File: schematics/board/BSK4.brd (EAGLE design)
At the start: 82 x 100 mm, 32 parts

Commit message: Подписаны разъемы на платах
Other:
- board text added: "to BSK1"
- board text added: "to PAYLOAD"
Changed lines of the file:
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@@
 <text x="54.1" y="4.9" size="1.778" layer="26" rot="MR0">BSK4 "Концерн ИТС"</text>
 <circle x="41" y="50" radius="15.25" width="0.2" layer="20"/>
+<text x="32" y="95" size="1.778" layer="26" rot="MR0">to BSK1</text>
+<text x="45" y="26" size="1.778" layer="26" rot="MR0">to PAYLOAD</text>
 </plain>
 <attributes>

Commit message: Платы подготовлены для Резонита
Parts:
- removed U$10: FS8205A+, CanCubeSat:FS8205A+
- added FS8205A#2: FS8205A+, CanCubeSat:FS8205A+
- moved R5 10.0 mm to (26.0, 21.0)
- moved LED1 9.90 mm to (68.9, 52.5), turned to 90 degrees
- moved R1 9.53 mm to (68.9, 50.6)
- moved LED5 7.32 mm to (26.0, 22.8), turned to 90 degrees
- moved R81 6.75 mm to (68.9, 48.4)
- moved LED4 4.19 mm to (31.3, 75.7)
- moved LED2 3.93 mm to (68.9, 46.5), turned to 270 degrees
- moved R3 2.47 mm to (11.2, 65.6)
- moved LED3 1.17 mm to (12.9, 65.6), turned to 0 degrees
- moved R2 1.00 mm to (25.3, 87.3)
- moved R7 1.00 mm to (25.3, 81.9)
- moved R4 0.51 mm to (33.0, 75.7)
- renumbered U$5 to DS18B20Z, U$8 to L293DD, U$9 to FS8205A#1
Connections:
- removed net HEAT: DS18B20Z.HEAT, FS8205A#1.HEAT, L293DD.HEAT, U$10.HEAT
- net GND: now also DS18B20Z.HEAT, FS8205A#1.HEAT, FS8205A#2.67, FS8205A#2.HEAT, L293DD.HEAT; no longer U$10.67
- net N$4: now also FS8205A#2.4; no longer U$10.4
- net N$6: now also FS8205A#2.5; no longer U$10.5
- net PL-: now also FS8205A#2.23; no longer U$10.23
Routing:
- net GND: track 128.6 -> 75.2 mm, vias 5 -> 2
- net N$27: track 13.8 -> 1.74 mm, vias 2 -> 0
- net 5V: track 165.6 -> 174.7 mm
- net N$3: track 59.1 -> 67.3 mm
- net N$2: track 72.6 -> 76.4 mm
- net PL-: track 76.6 -> 80.3 mm
- net BUS-: track 53.5 -> 50.4 mm
- net N$1: track 66.9 -> 69.2 mm
- net PL_KVCC: track 29.3 -> 30.3 mm
- net N$5: track 1.27 -> 1.94 mm
- net N$28: track 1.30 -> 1.84 mm
- added copper zone on layer 1, net GND
- removed copper zone on layer 1, net HEAT
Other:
- board text added: "BUS"
- board text added: "EM+"
- board text added: "EM-"
- board text added: "HEATER"
- board text added: "PL"

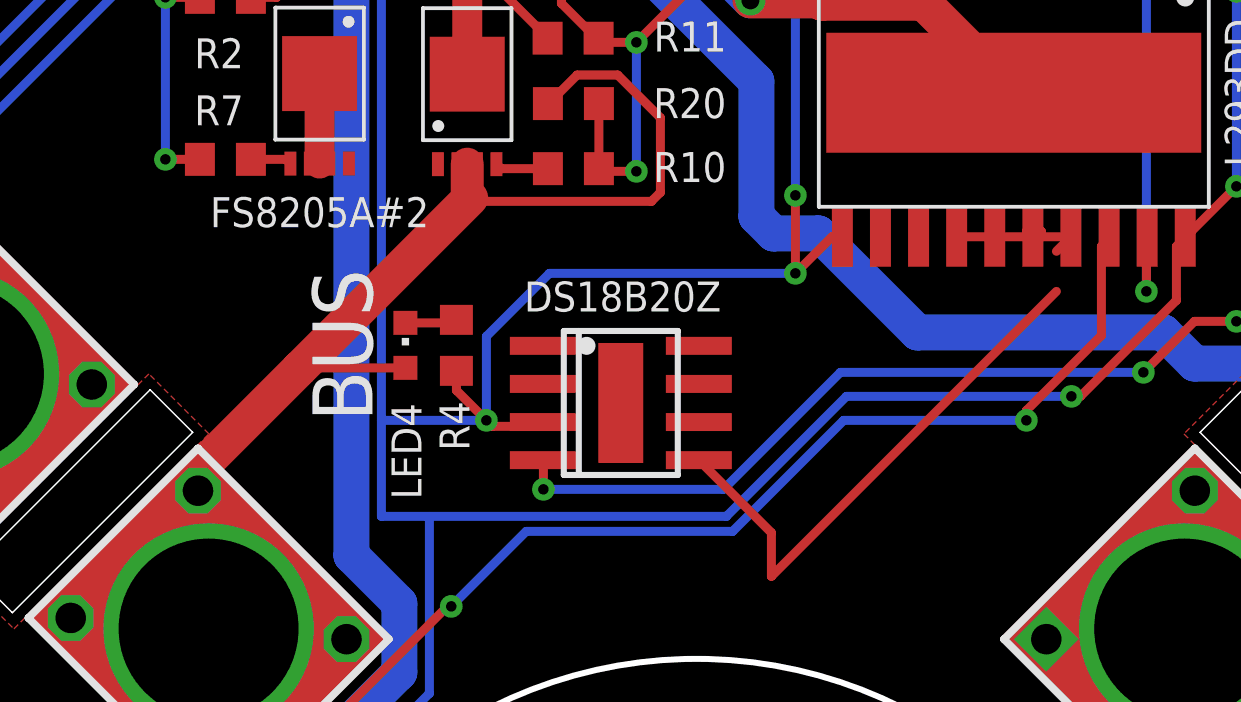
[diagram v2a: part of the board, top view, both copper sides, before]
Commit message: Исправлены RADIO и диоды
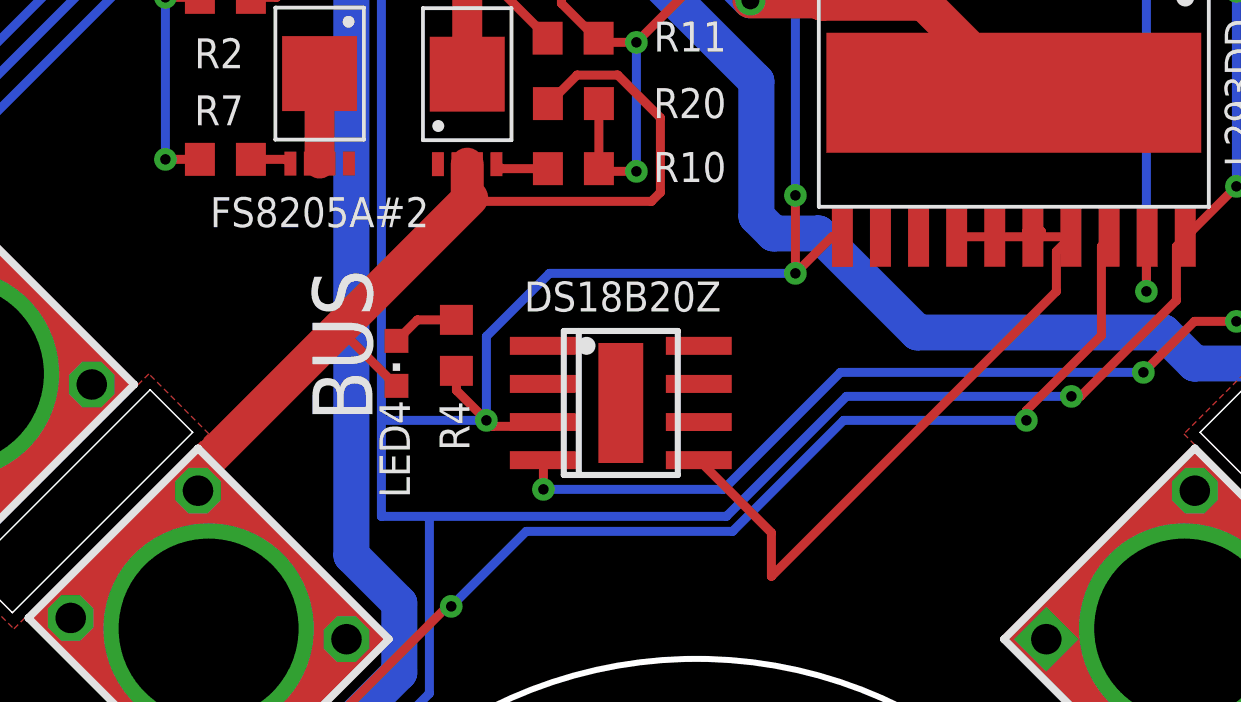
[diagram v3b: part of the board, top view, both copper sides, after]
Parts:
- moved LED4 0.67 mm to (31.0, 75.1), turned to 180 degrees
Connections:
- net BUS-: now also LED4.C; no longer LED4.A
- net N$27: now also LED4.A; no longer LED4.C
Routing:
- net GND: track 75.2 -> 76.6 mm
- net BUS-: track 50.4 -> 49.7 mm
- net N$27: track 1.74 -> 2.29 mm
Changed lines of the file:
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@@
 <attribute name="VALUE" x="14.805" y="64.33" size="1.27" layer="27" rot="R90"/>
-</element>
-<element name="LED4" library="led" library_urn="urn:adsk.eagle:library:259" package="CHIPLED_0603" package3d_urn="urn:adsk.eagle:package:15822/2" value="" x="31.3" y="75.7" smashed="yes">
-<attribute name="NAME" x="30.835" y="73.77" size="1" layer="25" rot="R270"/>
-<attribute name="POPULARITY" value="28" x="10.3" y="72.7" size="1.778" layer="27" display="off"/>
-<attribute name="VALUE" x="33.205" y="74.43" size="1.27" layer="27" rot="R90"/>
 </element>
 <element name="R4" library="resistor" library_urn="urn:adsk.eagle:library:348" package="R0603" package3d_urn="urn:adsk.eagle:package:23555/3" value="2k" x="33" y="75.7" smashed="yes" rot="R90">
@@
 <element name="R5" library="resistor" library_urn="urn:adsk.eagle:library:348" package="R0603" package3d_urn="urn:adsk.eagle:package:23555/3" value="2k" x="26" y="21" smashed="yes" rot="R180">
 <attribute name="NAME" x="24.235" y="21.465" size="1" layer="25" rot="R180"/>
+</element>
+<element name="LED4" library="led" library_urn="urn:adsk.eagle:library:259" package="CHIPLED_0603" package3d_urn="urn:adsk.eagle:package:15822/2" value="" x="31" y="75.1" smashed="yes" rot="R180">
+<attribute name="NAME" x="30.435" y="73.87" size="1.016" layer="25" rot="R270"/>
+<attribute name="POPULARITY" value="28" x="35.9" y="69.5" size="1.778" layer="27" rot="R180" display="off"/>
+<attribute name="VALUE" x="29.095" y="76.37" size="1.27" layer="27" rot="R270"/>
 </element>
 </elements>
@@
 <wire x1="48.58" y1="87.12" x2="51.58" y2="84.12" width="1.2" layer="1"/>
 <wire x1="45.18363125" y1="87.12" x2="48.58" y2="87.12" width="1.2" layer="1"/>
+<wire x1="53" y1="77.5" x2="53" y2="78.835" width="0.3" layer="1"/>
 </signal>
 <signal name="5V">
@@
 <wire x1="39.8" y1="83.28765625" x2="39.8" y2="80.8" width="0.3" layer="1"/>
 <wire x1="39.5" y1="80.5" x2="39.8" y2="80.8" width="0.3" layer="1"/>
-<wire x1="33.46" y1="80.6125625" x2="27.77371875" y2="74.92628125" width="1.2" layer="1"/>
-<wire x1="27.77371875" y1="74.92628125" x2="24.38644375" y2="71.53900625" width="1.2" layer="1"/>
+<wire x1="33.46" y1="80.6125625" x2="29.37371875" y2="76.52628125" width="1.2" layer="1"/>
+<wire x1="29.37371875" y1="76.52628125" x2="24.38644375" y2="71.53900625" width="1.2" layer="1"/>
 <wire x1="33.36" y1="80.7125625" x2="33.46" y2="80.6125625" width="0.3" layer="1"/>
 <wire x1="33.46" y1="80.6125625" x2="33.5725625" y2="80.5" width="0.3" layer="1"/>
 <wire x1="33.5725625" y1="80.5" x2="39.5" y2="80.5" width="0.3" layer="1"/>
-<contactref element="LED4" pad="A"/>
 <wire x1="33.36" y1="80.7125625" x2="33.36" y2="81.74" width="1.1" layer="1"/>
 <wire x1="24.38644375" y1="71.53900625" x2="24.38644375" y2="70.85619375" width="1" layer="1"/>
-<wire x1="31.3" y1="74.95" x2="27.7974375" y2="74.95" width="0.3" layer="1"/>
-<wire x1="27.7974375" y1="74.95" x2="27.77371875" y2="74.92628125" width="0.3" layer="1"/>
+<contactref element="LED4" pad="C"/>
+<wire x1="29.37371875" y1="76.52628125" x2="29.37371875" y2="75.97628125" width="0.3" layer="1"/>
+<wire x1="29.37371875" y1="75.97628125" x2="31" y2="74.35" width="0.3" layer="1"/>
 </signal>
 <signal name="N$8">
@@
 <wire x1="11.3" y1="66.35" x2="12.9" y2="66.35" width="0.3" layer="1"/>
 </signal>
-<signal name="N$27">
-<contactref element="R4" pad="2"/>
-<contactref element="LED4" pad="C"/>
-<wire x1="33" y1="76.55" x2="32.9" y2="76.45" width="0.3" layer="1"/>
-<wire x1="32.9" y1="76.45" x2="31.3" y2="76.45" width="0.3" layer="1"/>
-</signal>
 <signal name="N$28">
 <contactref element="R5" pad="2"/>
@@
 <wire x1="25.25" y1="21.1" x2="25.15" y2="21" width="0.3" layer="1"/>
 </signal>
+<signal name="N$27">
+<contactref element="LED4" pad="A"/>
+<contactref element="R4" pad="2"/>
+<wire x1="31" y1="75.85" x2="31.7" y2="76.55" width="0.3" layer="1"/>
+<wire x1="31.7" y1="76.55" x2="33" y2="76.55" width="0.3" layer="1"/>
+</signal>
 </signals>

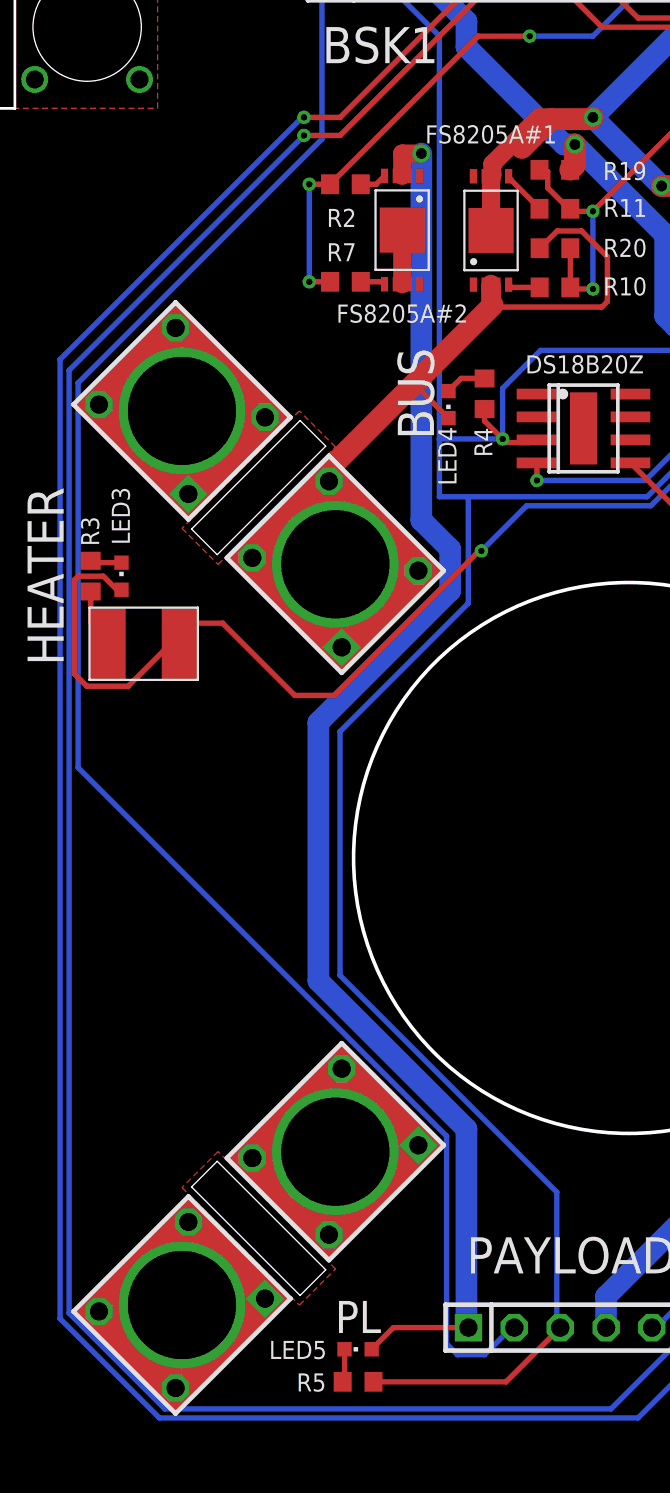
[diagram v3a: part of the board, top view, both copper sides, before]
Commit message: Резисторы у FS8205A 100Ом
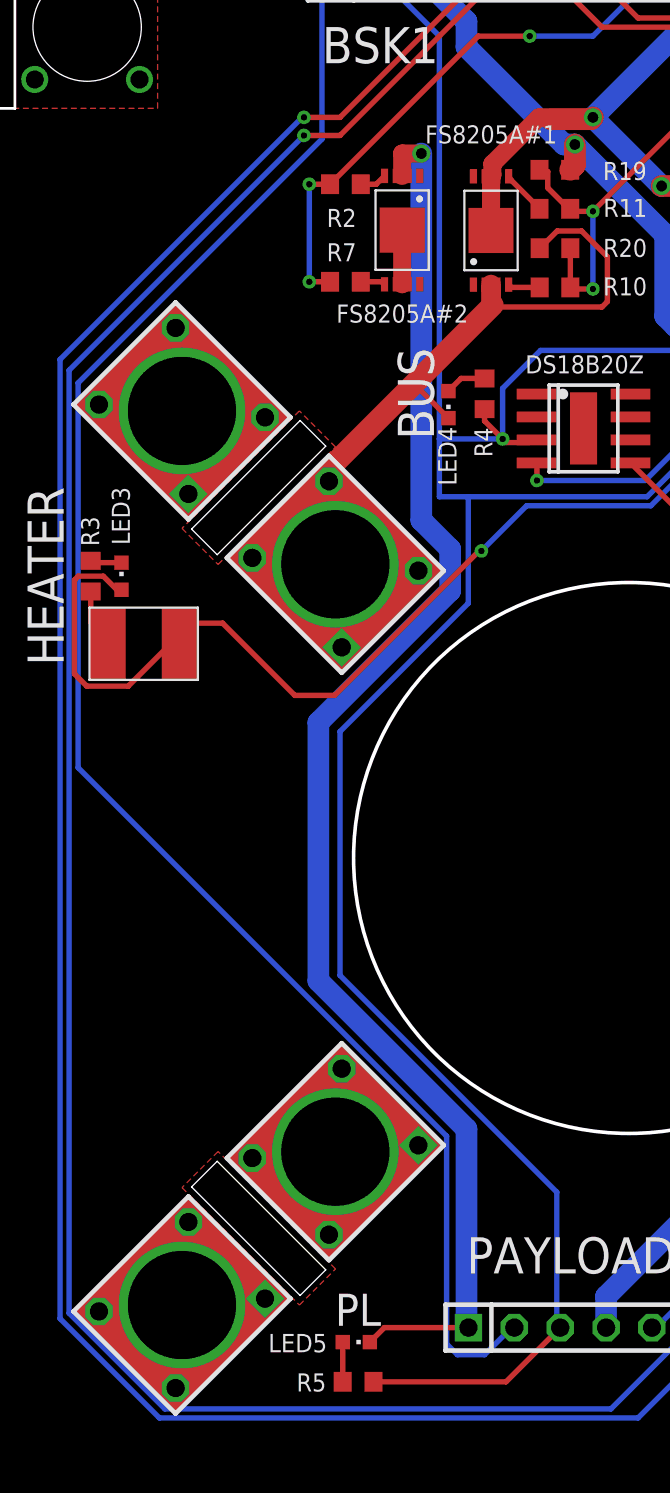
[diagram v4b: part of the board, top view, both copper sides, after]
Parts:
- R10, R11, R2, R7: value 10k -> 100R
- moved LED5 0.41 mm to (25.9, 23.2), turned to 270 degrees
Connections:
- net N$28: now also LED5.A; no longer LED5.C
- net PL-: now also LED5.C; no longer LED5.A
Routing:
- net GND: track 76.6 -> 74.1 mm
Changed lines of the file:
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@@
 <text x="68.9" y="53.4" size="2" layer="25" align="bottom-center">EM+</text>
 <text x="68.9" y="45.6" size="2" layer="25" rot="R180" align="bottom-center">EM-</text>
-<text x="26" y="23.7" size="1.778" layer="21" align="bottom-center">PL</text>
+<text x="26" y="24.1" size="1.778" layer="21" align="bottom-center">PL</text>
 </plain>
 <attributes>
@@
 </autorouter>
 <elements>
-<element name="R10" library="resistor" library_urn="urn:adsk.eagle:library:348" package="R0603" package3d_urn="urn:adsk.eagle:package:23555/3" value="10k" x="36.9" y="81.59" smashed="yes" rot="R180">
+<element name="R10" library="resistor" library_urn="urn:adsk.eagle:library:348" package="R0603" package3d_urn="urn:adsk.eagle:package:23555/3" value="100R" x="36.9" y="81.59" smashed="yes" rot="R180">
 <attribute name="NAME" x="39.565" y="81.145" size="1" layer="25"/>
 </element>
-<element name="R11" library="resistor" library_urn="urn:adsk.eagle:library:348" package="R0603" package3d_urn="urn:adsk.eagle:package:23555/3" value="10k" x="36.89" y="85.94" smashed="yes" rot="R180">
+<element name="R11" library="resistor" library_urn="urn:adsk.eagle:library:348" package="R0603" package3d_urn="urn:adsk.eagle:package:23555/3" value="100R" x="36.89" y="85.94" smashed="yes" rot="R180">
 <attribute name="NAME" x="39.575" y="85.495" size="1" layer="25"/>
 </element>
@@
 <attribute name="NAME" x="33.36" y="90.56" size="1" layer="25" rot="R180" align="bottom-center"/>
 </element>
-<element name="R2" library="resistor" library_urn="urn:adsk.eagle:library:348" package="R0603" package3d_urn="urn:adsk.eagle:package:23555/3" value="10k" x="25.3" y="87.3" smashed="yes">
+<element name="R2" library="resistor" library_urn="urn:adsk.eagle:library:348" package="R0603" package3d_urn="urn:adsk.eagle:package:23555/3" value="100R" x="25.3" y="87.3" smashed="yes">
 <attribute name="NAME" x="24.265" y="84.935" size="1" layer="25"/>
 </element>
-<element name="R7" library="resistor" library_urn="urn:adsk.eagle:library:348" package="R0603" package3d_urn="urn:adsk.eagle:package:23555/3" value="10k" x="25.3" y="81.9" smashed="yes">
+<element name="R7" library="resistor" library_urn="urn:adsk.eagle:library:348" package="R0603" package3d_urn="urn:adsk.eagle:package:23555/3" value="100R" x="25.3" y="81.9" smashed="yes">
 <attribute name="NAME" x="24.265" y="83.035" size="1" layer="25"/>
 </element>
@@
 <attribute name="NAME" x="32.435" y="73.835" size="1" layer="25" rot="R270"/>
 </element>
-<element name="LED5" library="led" library_urn="urn:adsk.eagle:library:259" package="CHIPLED_0603" package3d_urn="urn:adsk.eagle:package:15822/2" value="" x="26" y="22.8" smashed="yes" rot="R90">
-<attribute name="NAME" x="24.27" y="23.265" size="1" layer="25" rot="R180"/>
-<attribute name="POPULARITY" value="28" x="19" y="16.8" size="1.778" layer="27" rot="R90" display="off"/>
-<attribute name="VALUE" x="27.27" y="24.705" size="1.27" layer="27" rot="R180"/>
-</element>
 <element name="R5" library="resistor" library_urn="urn:adsk.eagle:library:348" package="R0603" package3d_urn="urn:adsk.eagle:package:23555/3" value="2k" x="26" y="21" smashed="yes" rot="R180">
 <attribute name="NAME" x="24.235" y="21.465" size="1" layer="25" rot="R180"/>
@@
 <attribute name="POPULARITY" value="28" x="35.9" y="69.5" size="1.778" layer="27" rot="R180" display="off"/>
 <attribute name="VALUE" x="29.095" y="76.37" size="1.27" layer="27" rot="R270"/>
+</element>
+<element name="LED5" library="led" library_urn="urn:adsk.eagle:library:259" package="CHIPLED_0603" package3d_urn="urn:adsk.eagle:package:15822/2" value="" x="25.9" y="23.2" smashed="yes" rot="R270">
+<attribute name="NAME" x="21.03" y="22.635" size="1.016" layer="25"/>
+<attribute name="POPULARITY" value="28" x="31.5" y="28.1" size="1.778" layer="27" rot="R270" display="off"/>
+<attribute name="VALUE" x="24.63" y="21.295" size="1.27" layer="27"/>
 </element>
 </elements>
@@
 <wire x1="52.5" y1="79.5" x2="52" y2="79.5" width="0.3" layer="1"/>
 <wire x1="52" y1="79.5" x2="52.215" y2="79.32" width="0.3" layer="1"/>
-<wire x1="12.5" y1="62" x2="12.325046875" y2="61.933803125" width="0.3" layer="1"/>
 <wire x1="12.325046875" y1="61.933803125" x2="12.13" y2="61.86" width="0.3" layer="1"/>
 <wire x1="53" y1="78.835" x2="53.485" y2="79.32" width="0.3" layer="1"/>
@@
 <wire x1="39" y1="91" x2="38.9" y2="90.9" width="1.2" layer="1"/>
 <wire x1="38.9" y1="90.9" x2="36.65863125" y2="90.9" width="1.2" layer="1"/>
-<wire x1="36.65863125" y1="90.9" x2="35.05863125" y2="89.3" width="1.2" layer="1"/>
 <polygon width="0.1524" layer="1" pour="cutout">
 <vertex x="16.25" y="68.25"/>
@@
 <wire x1="31.0976" y1="67.1024" x2="29.5" y2="68.7" width="1.2" layer="16"/>
 <wire x1="29.5" y1="68.7" x2="29.5" y2="89" width="1.2" layer="16"/>
-<contactref element="LED5" pad="A"/>
 <wire x1="28.44" y1="87.76" x2="28.44" y2="89" width="1" layer="1"/>
 <wire x1="28.44" y1="89" x2="29.5" y2="89" width="1" layer="1"/>
-<wire x1="26.75" y1="22.8" x2="27.95" y2="24" width="0.3" layer="1"/>
-<wire x1="27.95" y1="24" x2="32.11" y2="24" width="0.3" layer="1"/>
+<contactref element="LED5" pad="C"/>
+<wire x1="27.45" y1="24" x2="26.65" y2="23.2" width="0.3" layer="1"/>
+<wire x1="32.11" y1="24" x2="27.45" y2="24" width="0.3" layer="1"/>
 </signal>
 <signal name="N$11">
@@
 <wire x1="11.3" y1="66.35" x2="12.9" y2="66.35" width="0.3" layer="1"/>
 </signal>
-<signal name="N$28">
-<contactref element="R5" pad="2"/>
-<contactref element="LED5" pad="C"/>
-<wire x1="25.25" y1="22.8" x2="25.25" y2="21.1" width="0.3" layer="1"/>
-<wire x1="25.25" y1="21.1" x2="25.15" y2="21" width="0.3" layer="1"/>
-</signal>
 <signal name="N$27">
 <contactref element="LED4" pad="A"/>
@@
 <wire x1="31.7" y1="76.55" x2="33" y2="76.55" width="0.3" layer="1"/>
 </signal>
+<signal name="N$28">
+<contactref element="LED5" pad="A"/>
+<contactref element="R5" pad="2"/>
+<wire x1="25.15" y1="23.2" x2="25.15" y2="21" width="0.3" layer="1"/>
+</signal>
 </signals>

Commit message: Добавлены новые диоды
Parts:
- added LAP4: LAP4-BOTTOM, led:P47F-BOTTOM
- moved R5 3.16 mm to (29.1, 20.4)
- moved LED5 3.16 mm to (29.0, 22.6)
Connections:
- net BUS-: now also LAP4.C
- net N$27: now also LAP4.A
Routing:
- net N$27: track 2.29 -> 111.6 mm, vias 0 -> 4
- net BUS-: track 49.7 -> 110.4 mm, vias 0 -> 3
- net VDD: track 94.6 -> 112.5 mm
- net I2CINT: track 125.0 -> 128.4 mm
- net TIME: track 131.6 -> 135.0 mm
- net 5V: track 174.7 -> 171.9 mm
- net PL-: track 80.3 -> 77.4 mm
